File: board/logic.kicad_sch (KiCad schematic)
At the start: 0 parts

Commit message: add: Hierarchical Sheets
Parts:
- added C5, C7, C8: 100n, Capacitor_SMD:C_0603_1608Metric, symbol Device:C
- added R10, R11, R12, R13, R14, R15, R3, R4, R5, R6, R7, R8, R9: 100k, Resistor_SMD:R_0603_1608Metric, symbol Device:R_US
- added R16: 1k, Resistor_SMD:R_0603_1608Metric, symbol Device:R_US
- added R17: 8k2, Resistor_SMD:R_0603_1608Metric, symbol Device:R_US
- added U1, U3: 4040, Package_SO:SO-16_3.9x9.9mm_P1.27mm, symbol 4xxx:4040
- added U4: LM741, Package_SO:SOIC-8_3.9x4.9mm_P1.27mm, symbol Amplifier_Operational:LM741
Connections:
- new net: R12.1, U1.14 (Q9)
- new net: R10.2, R11.2, R12.2, R13.2, R14.2, R15.2, R3.2, R4.2, R5.2, R6.2, R7.2, R8.2, R9.2, U4.3 (+)
- new net: U3.10 (CLK), U4.6
- new net: R3.1, U1.9 (Q0)
- new net: R10.1, U1.13 (Q7)
- new net: R16.1, R17.2, U4.2 (-)
- new net: R11.1, U1.12 (Q8)
- new net: R8.1, U1.2 (Q5)
- new net: R5.1, U1.6 (Q2)
- new net: R9.1, U1.4 (Q6)
- new net: R15.1, U1.1 (Q11)
- new net: R13.1, U1.15 (Q10)
- new net: R7.1, U1.3 (Q4)
- new net: R6.1, U1.5 (Q3)
- new net: R4.1, U1.7 (Q1)
- new net 5V: C5.1, C7.1, C8.1, R16.2, U1.16 (VDD), U3.16 (VDD), U4.7 (V+)
- new net ALARM: U3.1 (Q11)
- new net CLOCK: U1.11 (Reset)
- new net GND: C5.2, C7.2, C8.2, R14.1, R17.1, U1.8 (VSS), U3.8 (VSS), U4.4 (V-)
- new net RESET: U1.10 (CLK), U3.11 (Reset)
- no-connect marks 0 -> 13

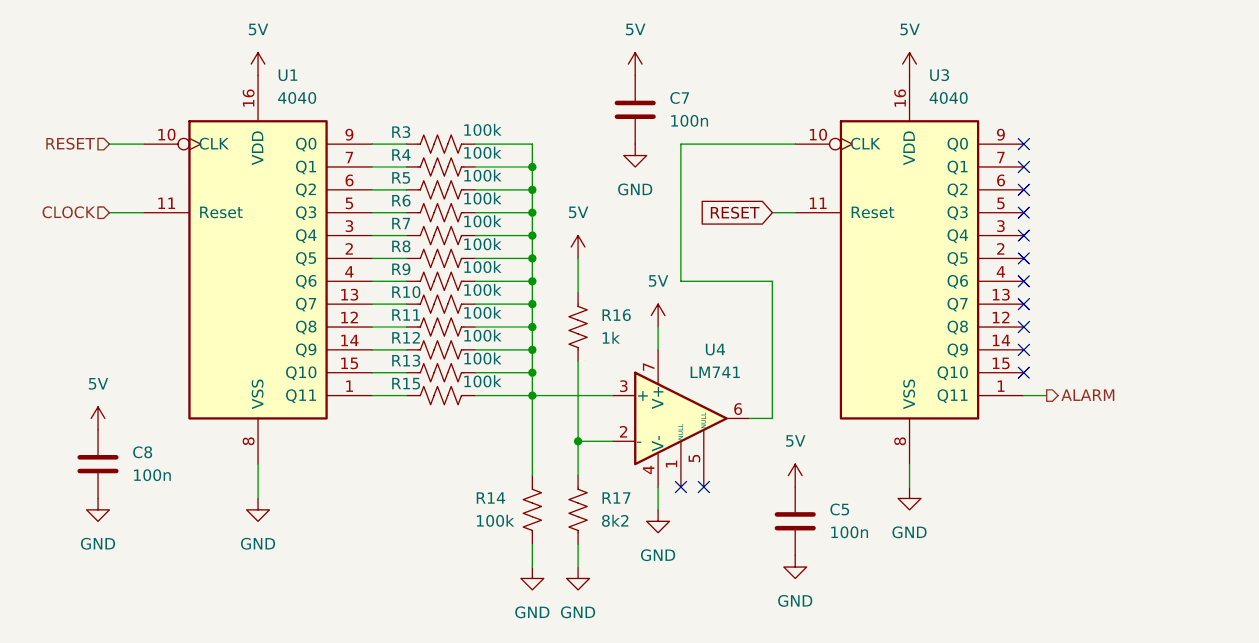
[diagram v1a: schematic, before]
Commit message: add: Mounting holes, box comments
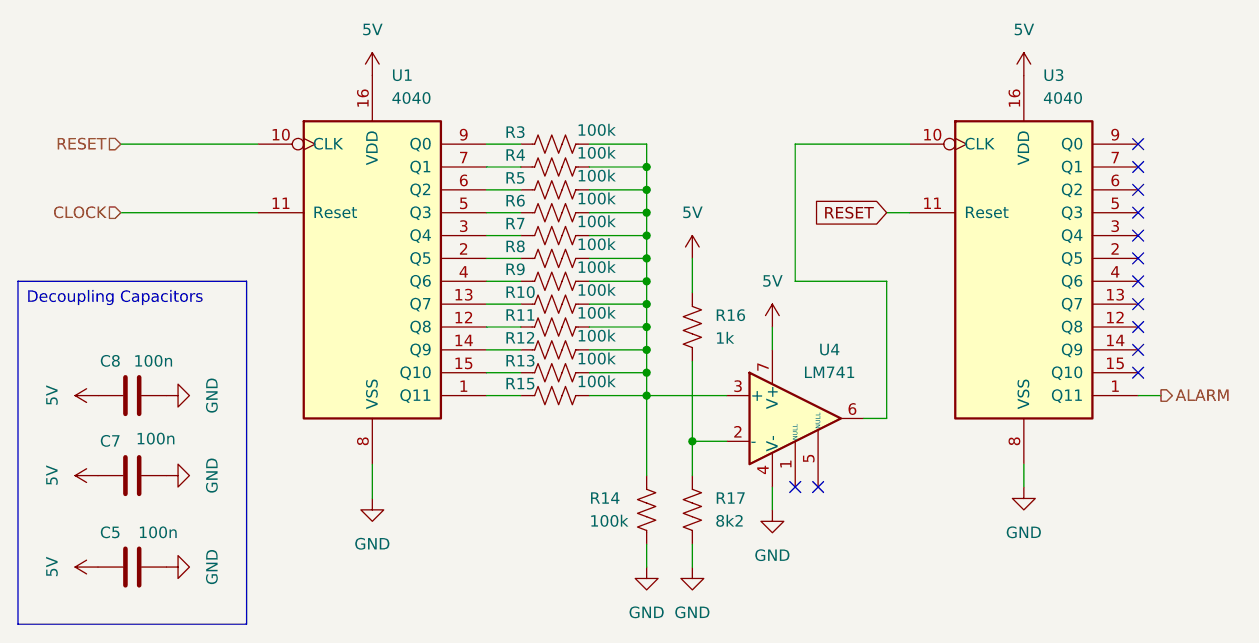
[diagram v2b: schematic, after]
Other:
- moved on the sheet: C5, C7, C8, R10, R11, R12, R13, R14, R15, R16, R17, R3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
